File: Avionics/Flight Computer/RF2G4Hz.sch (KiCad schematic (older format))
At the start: 39 parts, among them J5 734120110, U3 CC2650F128RGZR, U4 CC2592RGVR, Y5 XRCGB24M000F2P00R0

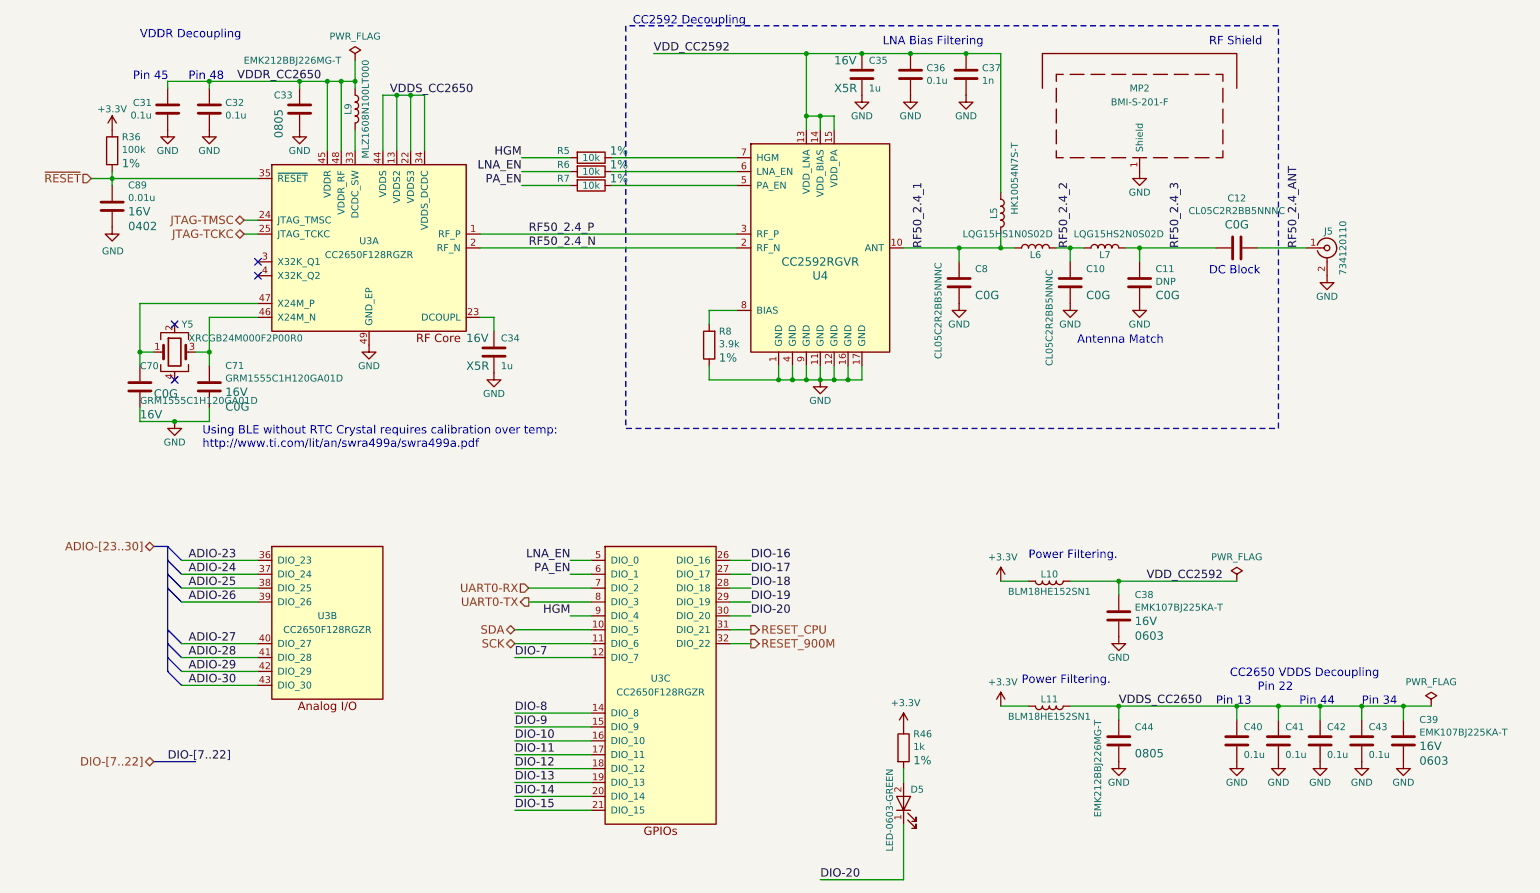
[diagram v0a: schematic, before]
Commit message: Updated more manufacturing part numbers for macrofab compatibility.
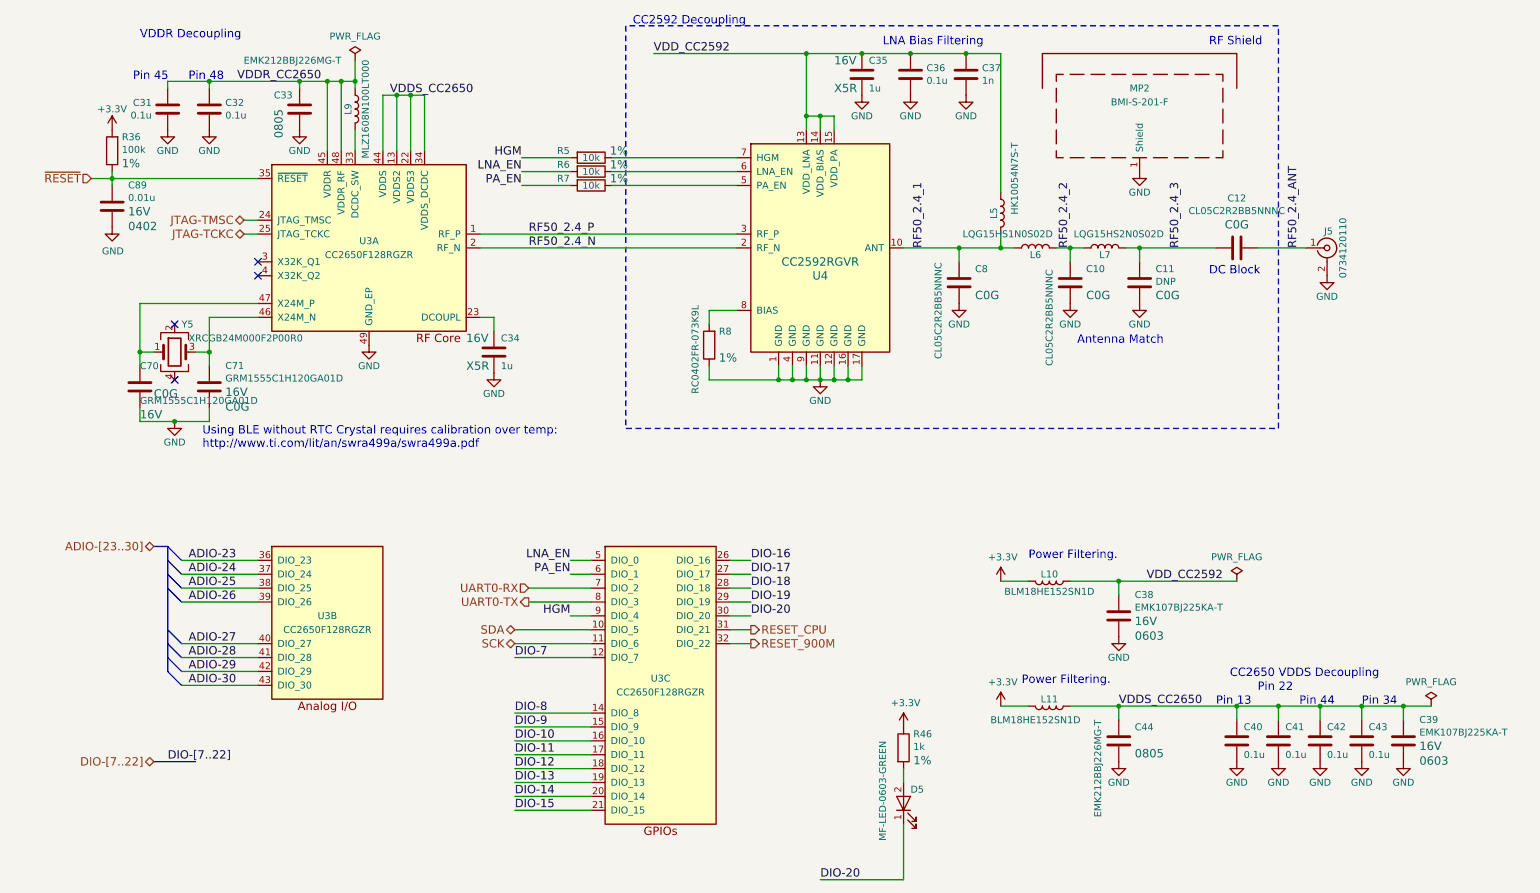
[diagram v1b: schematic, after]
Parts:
- D5: value LED-0603-GREEN -> MF-LED-0603-GREEN
- J5: value 734120110 -> 0734120110
- L10, L11: value BLM18HE152SN1 -> BLM18HE152SN1D
- R8: value 3.9k -> RC0402FR-073K9L
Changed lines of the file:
@@
 P 9750 2300
 F 0 "J5" H 9760 2420 50  0000 C CNN
-F 1 "734120110" V 9865 2300 50  0000 C CNN
+F 1 "0734120110" V 9865 2300 50  0000 C CNN
 F 2 "Connectors_Molex:Molex_Microcoaxial_RF" H 9750 2300 50  0001 C CNN
 F 3 "http://www.molex.com/pdm_docs/sd/734120110_sd.pdf" H 9750 2300 50  0001 C CNN
@@
 P 7750 4700
 F 0 "L10" V 7700 4700 50  0000 C CNN
-F 1 "BLM18HE152SN1" V 7825 4700 50  0000 C CNN
+F 1 "BLM18HE152SN1D" V 7825 4700 50  0000 C CNN
 F 2 "Inductors_SMD:L_0603" H 7750 4700 50  0001 C CNN
 F 3 "" H 7750 4700 50  0001 C CNN
@@
 P 7750 5600
 F 0 "L11" V 7700 5600 50  0000 C CNN
-F 1 "BLM18HE152SN1" V 7825 5600 50  0000 C CNN
+F 1 "BLM18HE152SN1D" V 7850 5500 50  0000 C CNN
 F 2 "Inductors_SMD:L_0603" H 7750 5600 50  0001 C CNN
 F 3 "" H 7750 5600 50  0001 C CNN
@@
 P 5300 3000
 F 0 "R8" H 5230 2901 50  0000 R CNN
-F 1 "3.9k" H 5230 2992 50  0000 R CNN
+F 1 "RC0402FR-073K9L" V 5400 3350 50  0000 R CNN
 F 2 "Resistors_SMD:R_0402" V 300 1700 50  0001 C CNN
 F 3 "" V 580 1700 50  0001 C CNN
@@
 P 6700 6300
 F 0 "D5" V 6800 6250 50  0000 R CNN
-F 1 "LED-0603-GREEN" H 6950 6400 50  0000 R CNN
+F 1 "MF-LED-0603-GREEN" H 7150 6450 50  0000 R CNN
 F 2 "LEDs:LED_0603" H 1300 -50 50  0001 C CNN
 F 3 "https://s3.amazonaws.com/mfprodpublic/datasheets/S_110_LTST-C190KGKT.pdf" H 1300 -50 50  0001 C CNN

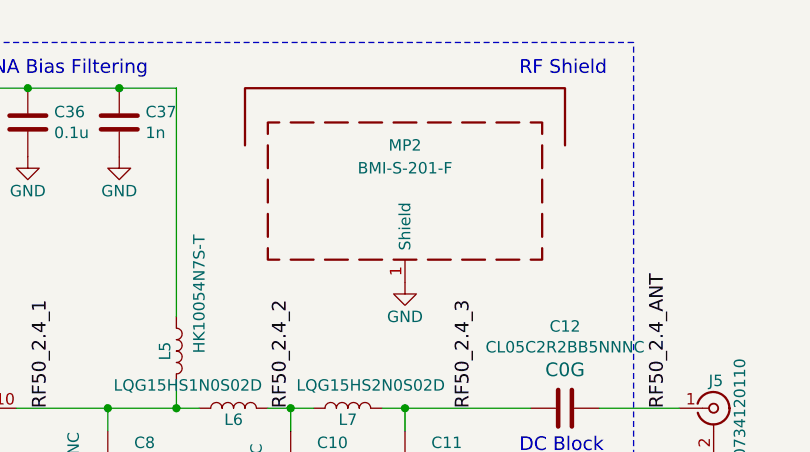
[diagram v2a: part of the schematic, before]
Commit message: Finished replacement and supply tuning
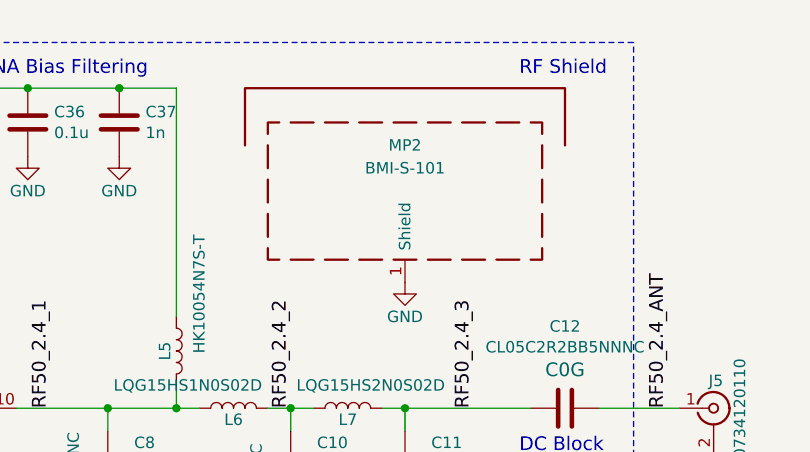
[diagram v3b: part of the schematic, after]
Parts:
- MP2: value BMI-S-201-F -> BMI-S-101; footprint Shielding_Cabinets:Laird_Technologies_BMI-S-201-F_13.66x12.70mm -> Shielding_Cabinets:Laird_Technologies_BMI-S-101_13.66x12.70mm
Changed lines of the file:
@@
 P 8400 1350
 F 0 "MP2" H 8400 1550 50  0000 C CNN
-F 1 "BMI-S-201-F" H 8400 1450 50  0000 C CNN
-F 2 "Shielding_Cabinets:Laird_Technologies_BMI-S-201-F_13.66x12.70mm" H 8400 1250 50  0001 C CNN
+F 1 "BMI-S-101" H 8400 1450 50  0000 C CNN
+F 2 "Shielding_Cabinets:Laird_Technologies_BMI-S-101_13.66x12.70mm" H 8400 1250 50  0001 C CNN
 F 3 "" H 8400 1250 50  0001 C CNN
 	1    8400 1350
